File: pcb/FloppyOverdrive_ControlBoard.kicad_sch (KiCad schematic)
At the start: 26 parts

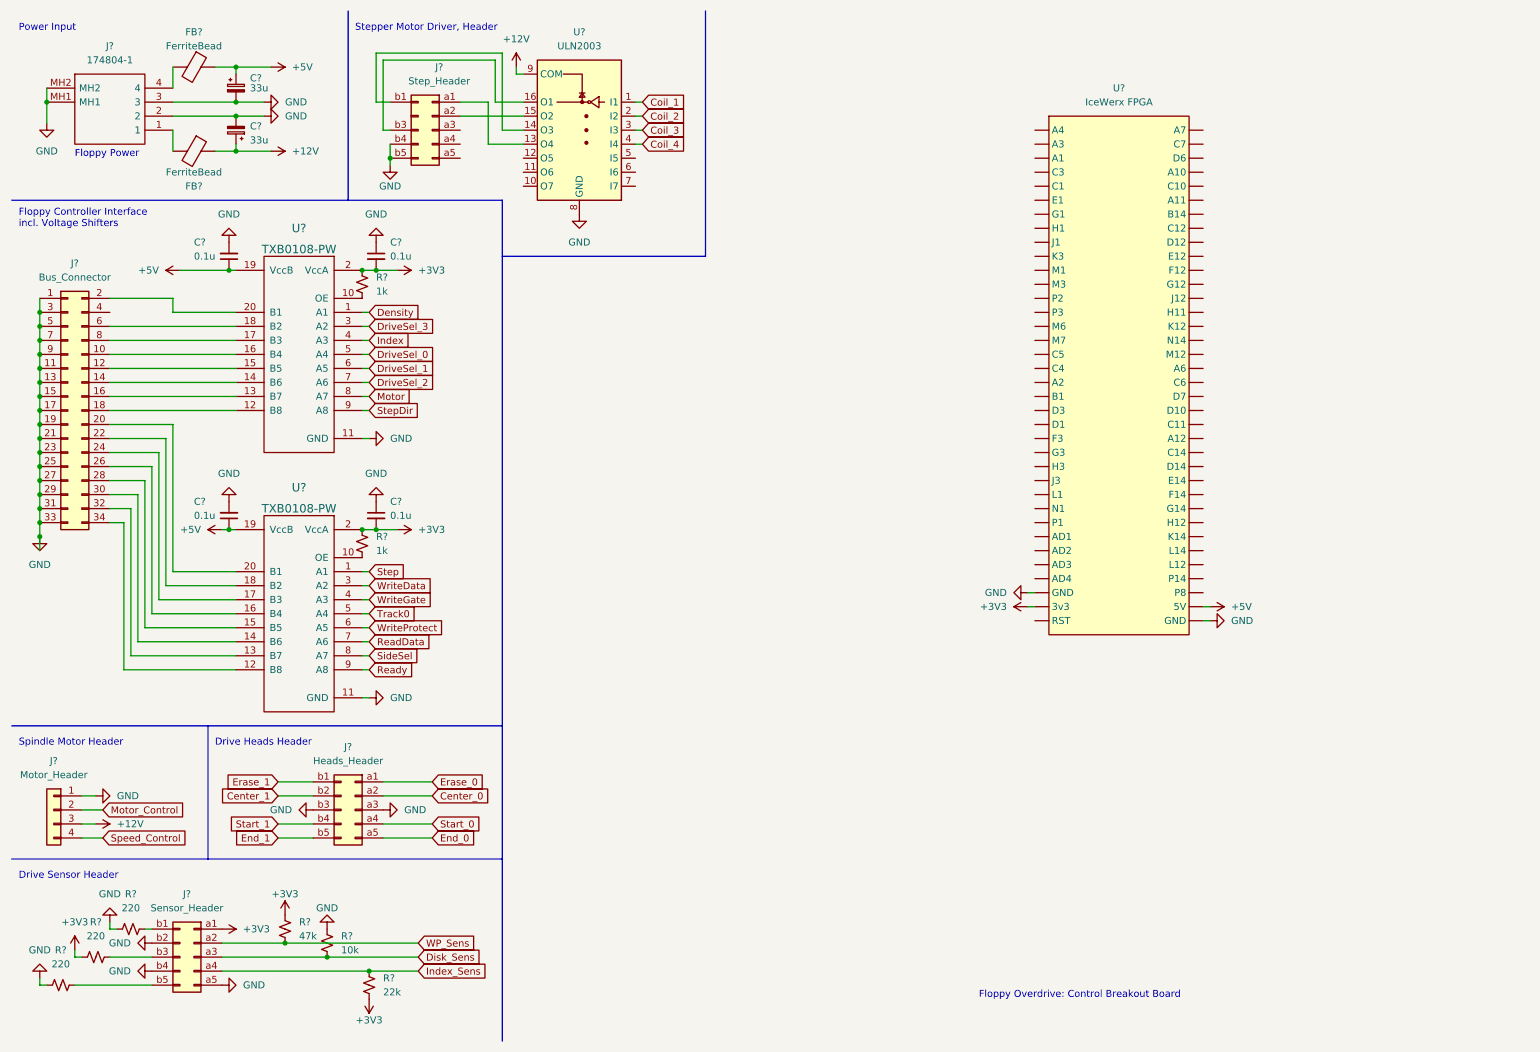
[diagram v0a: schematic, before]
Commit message: Add motor header files, outline for PCB
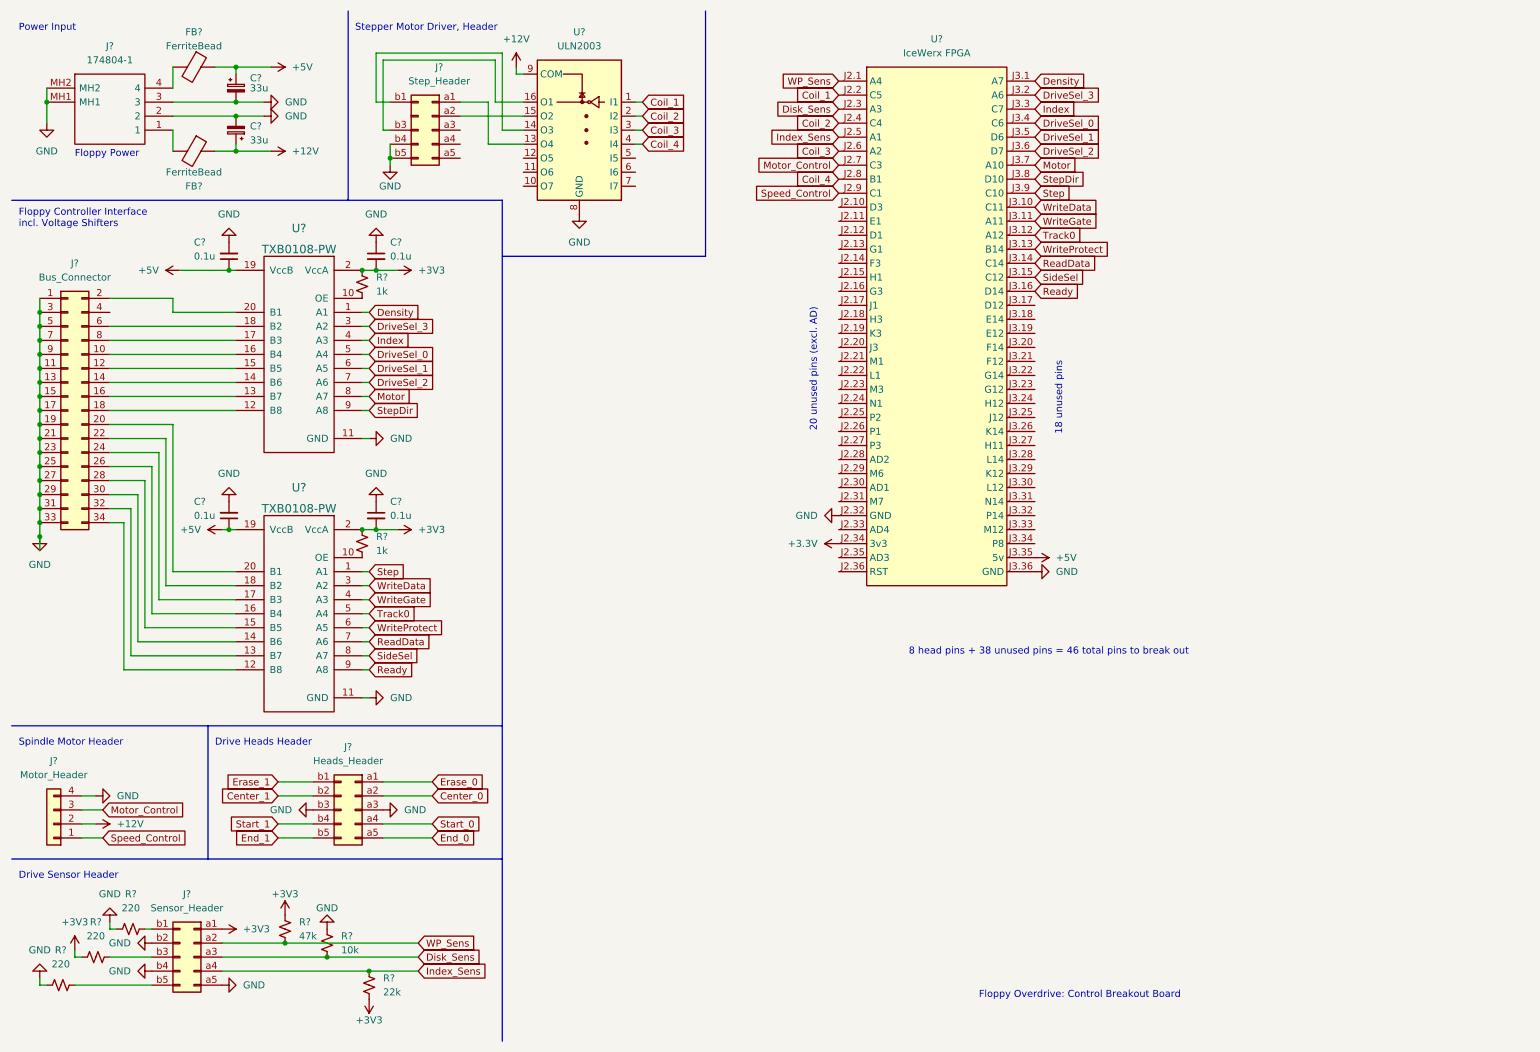
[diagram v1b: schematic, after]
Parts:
- removed U?: IceWerx FPGA, IceWerx:IceWerx FPGA, symbol IceWerx:IceWerx FPGA
- added U?: IceWerx FPGA, IceWerx:IceWerx FPGA, symbol IceWerx:IceWerx FPGA
- J? (x2): footprint (none) -> Connector_PinHeader_2.54mm:PinHeader_2x05_P2.54mm_Horizontal
- J?: footprint (none) -> 440055-4:SHDRRA4W50P15X200_1X4_1000X770X525P
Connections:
- net +12V: now also J?.2 (Pin_2); no longer J?.3 (Pin_3)
- net +5V: now also U?.J3.35 (5v)
- net Coil_1: now also U?.J2.2 (C5)
- net Coil_2: now also U?.J2.4 (C4)
- net Coil_3: now also U?.J2.6 (A2)
- net Coil_4: now also U?.J2.8 (B1)
- net Density: now also U?.J3.1 (A7)
- net Disk_Sens: now also U?.J2.3 (A3)
- net DriveSel_0: now also U?.J3.4 (C6)
- net DriveSel_1: now also U?.J3.5 (D6)
- net DriveSel_2: now also U?.J3.6 (D7)
- net DriveSel_3: now also U?.J3.2 (A6)
- net GND: now also J?.4 (Pin_4), U?.J2.32 (GND), U?.J3.36 (GND); no longer J?.1 (Pin_1)
- net Index: now also U?.J3.3 (C7)
- net Index_Sens: now also U?.J2.5 (A1)
- net Motor: now also U?.J3.7 (A10)
- net Motor_Control: now also J?.3 (Pin_3), U?.J2.7 (C3); no longer J?.2 (Pin_2)
- net ReadData: now also U?.J3.14 (C14)
- net Ready: now also U?.J3.16 (D14)
- net SideSel: now also U?.J3.15 (C12)
- net Speed_Control: now also J?.1 (Pin_1), U?.J2.9 (C1); no longer J?.4 (Pin_4)
- net Step: now also U?.J3.9 (C10)
- net StepDir: now also U?.J3.8 (D10)
- net Track0: now also U?.J3.12 (A12)
- net WP_Sens: now also U?.J2.1 (A4)
- net WriteData: now also U?.J3.10 (C11)
- net WriteGate: now also U?.J3.11 (A11)
- net WriteProtect: now also U?.J3.13 (B14)
- new net +3.3V: U?.J2.34 (3v3)
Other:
- note added: "18 unused pins"
- note added: "20 unused pins (excl. AD)"
- note added: "8 head pins + 38 unused pins = 46 total pins to break out"
- moved on the sheet: J?

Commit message: Added LEDs, footprints to PCB schematic
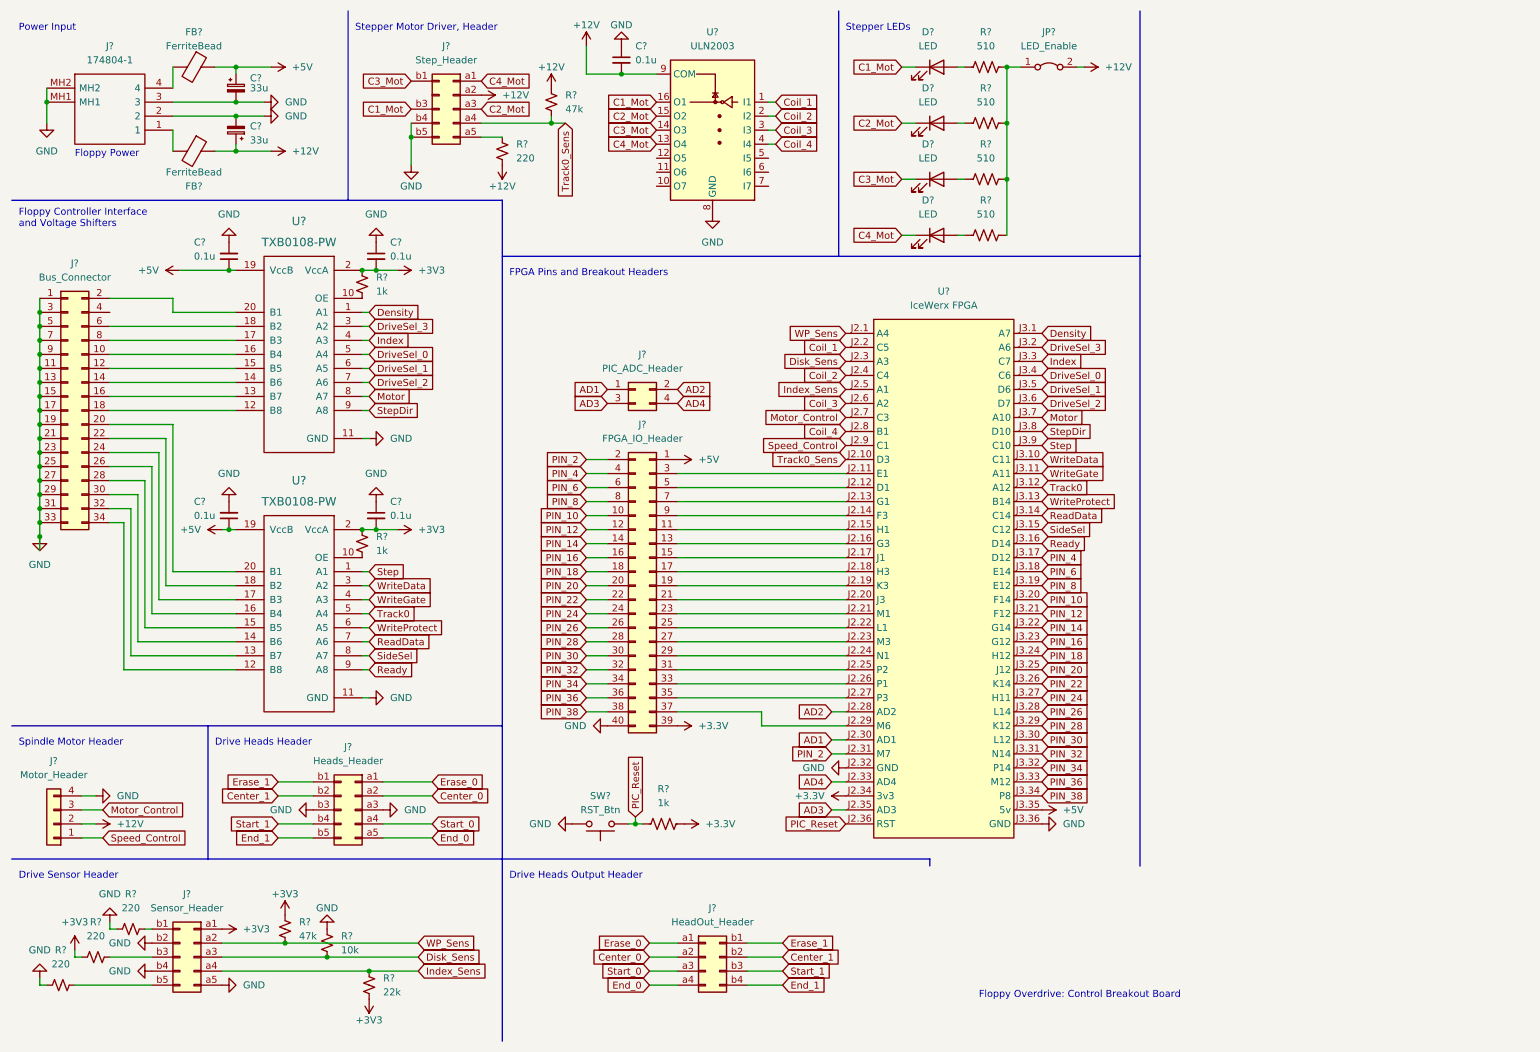
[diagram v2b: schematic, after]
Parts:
- added C?: 0.1u, Capacitor_THT:C_Disc_D5.0mm_W2.5mm_P2.50mm, symbol Device:C_Small
- added D? (x4): LED, LED_THT:LED_D5.0mm, symbol Device:LED
- added J?: HeadOut_Header, Connector_PinHeader_2.54mm:PinHeader_2x04_P2.54mm_Vertical, symbol Connector_Generic:Conn_02x04_Row_Letter_First
- added J?: PIC_ADC_Header, symbol Connector_Generic:Conn_02x02_Odd_Even
- added J?: FPGA_IO_Header, symbol Connector_Generic:Conn_02x20_Odd_Even
- added JP?: LED_Enable, Connector_PinHeader_2.54mm:PinHeader_1x02_P2.54mm_Vertical, symbol Jumper:Jumper_2_Bridged
- added R? (x4): 510, Resistor_THT:R_Axial_DIN0207_L6.3mm_D2.5mm_P10.16mm_Horizontal, symbol Device:R_US
- added R?: 220, Resistor_THT:R_Axial_DIN0207_L6.3mm_D2.5mm_P10.16mm_Horizontal, symbol Device:R_Small_US
- added R?: 47k, Resistor_THT:R_Axial_DIN0207_L6.3mm_D2.5mm_P10.16mm_Horizontal, symbol Device:R_Small_US
- added R?: 1k, Resistor_THT:R_Axial_DIN0207_L6.3mm_D2.5mm_P10.16mm_Horizontal, symbol Device:R_US
- added SW?: RST_Btn, Button_Switch_THT:SW_PUSH-12mm, symbol Switch:SW_Push
- C? (x2): footprint (none) -> Capacitor_THT:CP_Radial_D5.0mm_P2.00mm
- C? (x4): footprint (none) -> Capacitor_THT:C_Disc_D5.0mm_W2.5mm_P2.50mm
- FB? (x2): footprint (none) -> Resistor_SMD:R_1206_3216Metric
- J?: footprint (none) -> Connector_PinHeader_2.00mm:PinHeader_2x05_P2.00mm_Horizontal
- R? (x8): footprint (none) -> Resistor_THT:R_Axial_DIN0207_L6.3mm_D2.5mm_P10.16mm_Horizontal
- U? (x2): footprint (none) -> Package_SO:TSSOP-20_4.4x6.5mm_P0.65mm
- U?: footprint (none) -> Package_SO:TSSOP-16_4.4x5mm_P0.65mm
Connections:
- net +12V: now also J?.a2 (Pin_a2), C?.2, JP?.2 (B), R?.1, R?.2
- net +3.3V: now also J?.39 (Pin_39), R?.2
- net +5V: now also J?.1 (Pin_1)
- net Center_0: now also J?.a2 (Pin_a2)
- net Center_1: now also J?.b2 (Pin_b2)
- net End_0: now also J?.a4 (Pin_a4)
- net End_1: now also J?.b4 (Pin_b4)
- net Erase_0: now also J?.a1 (Pin_a1)
- net Erase_1: now also J?.b1 (Pin_b1)
- net GND: now also C?.1, J?.40 (Pin_40), SW?.2
- net Start_0: now also J?.a3 (Pin_a3)
- net Start_1: now also J?.b3 (Pin_b3)
- net C4_Mot: now reaches J?.a1 (Pin_a1), U?.13 (O4)
- net C4_Mot: now also D?.1 (K)
- net C2_Mot: now reaches U?.15 (O2)
- net C2_Mot: now also J?.a3 (Pin_a3), D?.1 (K); no longer J?.a2 (Pin_a2)
- net Track0_Sens: now reaches J?.a4 (Pin_a4)
- net Track0_Sens: now also U?.J2.10 (D3), R?.2
- net at J?.a5 (Pin_a5): now also R?.1
- net C3_Mot: now reaches J?.b1 (Pin_b1), U?.14 (O3)
- net C3_Mot: now also D?.1 (K)
- net C1_Mot: now reaches J?.b3 (Pin_b3), U?.16 (O1)
- net C1_Mot: now also D?.1 (K)
- net at U?.J2.11 (E1): now also J?.3 (Pin_3)
- net at U?.J2.12 (D1): now also J?.5 (Pin_5)
- net at U?.J2.13 (G1): now also J?.7 (Pin_7)
- net at U?.J2.14 (F3): now also J?.9 (Pin_9)
- net at U?.J2.15 (H1): now also J?.11 (Pin_11)
- net at U?.J2.16 (G3): now also J?.13 (Pin_13)
- net at U?.J2.17 (J1): now also J?.15 (Pin_15)
- net at U?.J2.18 (H3): now also J?.17 (Pin_17)
- net at U?.J2.19 (K3): now also J?.19 (Pin_19)
- net at U?.J2.20 (J3): now also J?.21 (Pin_21)
- net at U?.J2.21 (M1): now also J?.23 (Pin_23)
- net at U?.J2.22 (L1): now also J?.25 (Pin_25)
- net at U?.J2.23 (M3): now also J?.27 (Pin_27)
- net at U?.J2.24 (N1): now also J?.29 (Pin_29)
- net at U?.J2.25 (P2): now also J?.31 (Pin_31)
- net at U?.J2.26 (P1): now also J?.33 (Pin_33)
- net at U?.J2.27 (P3): now also J?.35 (Pin_35)
- net AD2: now reaches U?.J2.28 (AD2)
- net AD2: now also J?.2 (Pin_2)
- net at U?.J2.29 (M6): now also J?.37 (Pin_37)
- net AD1: now reaches U?.J2.30 (AD1)
- net AD1: now also J?.1 (Pin_1)
- net PIN_2: now reaches U?.J2.31 (M7)
- net PIN_2: now also J?.2 (Pin_2)
- net AD4: now reaches U?.J2.33 (AD4)
- net AD4: now also J?.4 (Pin_4)
- net AD3: now reaches U?.J2.35 (AD3)
- net AD3: now also J?.3 (Pin_3)
- net PIC_Reset: now reaches U?.J2.36 (RST)
- net PIC_Reset: now also R?.1, SW?.1
- net PIN_4: now reaches U?.J3.17 (D12)
- net PIN_4: now also J?.4 (Pin_4)
- net PIN_6: now reaches U?.J3.18 (E14)
- net PIN_6: now also J?.6 (Pin_6)
- net PIN_8: now reaches U?.J3.19 (E12)
- net PIN_8: now also J?.8 (Pin_8)
- net PIN_10: now reaches U?.J3.20 (F14)
- net PIN_10: now also J?.10 (Pin_10)
- net PIN_12: now reaches U?.J3.21 (F12)
- net PIN_12: now also J?.12 (Pin_12)
- net PIN_14: now reaches U?.J3.22 (G14)
- net PIN_14: now also J?.14 (Pin_14)
- net PIN_16: now reaches U?.J3.23 (G12)
- net PIN_16: now also J?.16 (Pin_16)
- net PIN_18: now reaches U?.J3.24 (H12)
- net PIN_18: now also J?.18 (Pin_18)
- net PIN_20: now reaches U?.J3.25 (J12)
- net PIN_20: now also J?.20 (Pin_20)
- net PIN_22: now reaches U?.J3.26 (K14)
- net PIN_22: now also J?.22 (Pin_22)
- net PIN_24: now reaches U?.J3.27 (H11)
- net PIN_24: now also J?.24 (Pin_24)
- net PIN_26: now reaches U?.J3.28 (L14)
- net PIN_26: now also J?.26 (Pin_26)
- net PIN_28: now reaches U?.J3.29 (K12)
- net PIN_28: now also J?.28 (Pin_28)
- net PIN_30: now reaches U?.J3.30 (L12)
- net PIN_30: now also J?.30 (Pin_30)
- net PIN_32: now reaches U?.J3.31 (N14)
- net PIN_32: now also J?.32 (Pin_32)
- net PIN_34: now reaches U?.J3.32 (P14)
- net PIN_34: now also J?.34 (Pin_34)
- net PIN_36: now reaches U?.J3.33 (M12)
- net PIN_36: now also J?.36 (Pin_36)
- net PIN_38: now reaches U?.J3.34 (P8)
- net PIN_38: now also J?.38 (Pin_38)
- new net: D?.2 (A), R?.1 (x4)
- new net: JP?.1 (A), R?.2, R?.2, R?.2, R?.2
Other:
- note added: "Drive Heads Output Header"
- note added: "FPGA Pins and Breakout Headers"
- note added: "Floppy Controller Interface and Voltage Shifters"
- note added: "Stepper LEDs"
- note removed: "18 unused pins"
- note removed: "20 unused pins (excl. AD)"
- note removed: "8 head pins + 38 unused pins = 46 total pins to break out"
- note removed: "Floppy Controller Interface incl. Voltage Shifters"
- moved on the sheet: J?, U?

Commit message: PCB Update
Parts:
- D1: renamed from D?; value LED -> LED1
- D2: renamed from D?; value LED -> LED2
- D3: renamed from D?; value LED -> LED3
- D4: renamed from D?; value LED -> LED4
- J3: renamed from J?; footprint (none) -> Connector_PinHeader_2.54mm:PinHeader_2x17_P2.54mm_Horizontal
- J7: renamed from J?; footprint (none) -> Connector_PinHeader_2.54mm:PinHeader_2x02_P2.54mm_Vertical
- J8: renamed from J?; footprint (none) -> Connector_PinHeader_2.54mm:PinHeader_2x20_P2.54mm_Vertical
- SW1: renamed from SW?; footprint Button_Switch_THT:SW_PUSH-12mm -> Button_Switch_THT:SW_PUSH_6mm
- gave numbers to parts that had none: 35
